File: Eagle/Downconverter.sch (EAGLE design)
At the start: 26 parts, among them J2 3.5HEADPHONEJACK, J5 U.FL_CONN, J6 U.FL_CONN, U1 5V_REG, U2 MIXER, U3 DUAL_OP_AMP_LMV822, U4 DIGITAL_POTDIGITAL_POT

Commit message: update
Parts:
- removed R1: 330, 764Library:R0603
- removed R2: 110, 764Library:R0603
- added C10: 100uF, 764Library:C0603
- added C11: 470pF, 764Library:C0603
- added C9: 10uF, 764Library:C0603
- added R10, R7, R8, R9: 1k, 764Library:R0603
- added U5: TC1185-3.3VCT713, 764Library:TC1185-3.3VCT713
- C3, C4: value 1uF -> 5.6uF
- C8: value 1uF -> 100uF; device 764Library:C0603 -> 764Library:EDK107M6R3A9GAA
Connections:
- removed net N$1: R1.2, R2.1, U1.GND
- removed net N$12: C8.1, U3B.OUT, U4.P0W
- new net AUDIO_OUTPUT: C8.2, J2.RING1, J2.RINGSWITCH, J2.TIP, J2.TIPSWITCH
- new net N$5: C11.1, U5.BYPASS
- net 3.3V: now also C10.1, C6.1, R10.1, R7.1, U3A.VDD, U5.VOUT; no longer J4.2
- net 5V: now also C9.1, U5.!SHDN, U5.VIN; no longer C6.1, R2.2, U3A.VDD
- net 9V: now also J4.2
- net GND: now also C10.2, C11.2, C9.2, R8.2, R9.2, U1.GND, U5.GND; no longer R1.1
- net N$4: now also R7.2, R8.1
- net N$8: now also R10.2, R9.1
- net RDR_OUT: now also C8.1, U3B.OUT, U4.P0W; no longer C8.2, J2.RING1, J2.RINGSWITCH, J2.TIP, J2.TIPSWITCH
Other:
- note added: "TC1185"
- note added: "To Source Module"
- note added: "To the ADC on the DSP Board. Biased on that board."
- note removed: "9V"
- note removed: "From Teensy - Digital Pot 3.3V Power"
- moved on the sheet: J3, J4, J7

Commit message: REV0 and GERBERS FTW
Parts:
- added C12, C13: 0.1uF, 764Library:C0603
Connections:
- net N$2 renamed IF
- net GND: now also C12.2, C13.2
- net N$13: now also R6.1
- net N$4: now also C12.1; no longer R4.1
- net N$8: now also C13.1; no longer R6.1
- net N$9: now also R4.1
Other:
- moved on the sheet: C3, R4, R6, R7, R8, R9

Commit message: Changes
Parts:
- C10, C2: value 100uF -> 1uF
- C3, C4: value 5.6uF -> 2.2uF
- R4, R6: value 1k -> 2.7k
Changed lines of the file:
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@@
 <part name="C1" library="764Library" deviceset="C0603" device="" package3d_urn="urn:adsk.eagle:package:26057/1" value="10uF"/>
 <part name="SUPPLY1" library="SparkFun-PowerSymbols" library_urn="urn:adsk.eagle:library:530" deviceset="5V" device=""/>
-<part name="C2" library="764Library" deviceset="C0603" device="" package3d_urn="urn:adsk.eagle:package:26057/1" value="100uF"/>
+<part name="C2" library="764Library" deviceset="C0603" device="" package3d_urn="urn:adsk.eagle:package:26057/1" value="1uF"/>
 <part name="GND3" library="SparkFun-PowerSymbols" library_urn="urn:adsk.eagle:library:530" deviceset="GND" device=""/>
 <part name="J3" library="SparkFun-Connectors" library_urn="urn:adsk.eagle:library:513" deviceset="CONN_02" device="" package3d_urn="urn:adsk.eagle:package:38039/1"/>
@@
 <part name="R3" library="764Library" deviceset="R0603" device="" package3d_urn="urn:adsk.eagle:package:26057/1" value="50"/>
 <part name="GND8" library="SparkFun-PowerSymbols" library_urn="urn:adsk.eagle:library:530" deviceset="GND" device=""/>
-<part name="C3" library="764Library" deviceset="C0603" device="" package3d_urn="urn:adsk.eagle:package:26057/1" value="5.6uF"/>
-<part name="R4" library="764Library" deviceset="R0603" device="" package3d_urn="urn:adsk.eagle:package:26057/1" value="1k"/>
+<part name="C3" library="764Library" deviceset="C0603" device="" package3d_urn="urn:adsk.eagle:package:26057/1" value="2.2uF"/>
+<part name="R4" library="764Library" deviceset="R0603" device="" package3d_urn="urn:adsk.eagle:package:26057/1" value="2.7k"/>
 <part name="U3" library="764Library" deviceset="DUAL_OP_AMP_LMV822" device=""/>
 <part name="GND9" library="SparkFun-PowerSymbols" library_urn="urn:adsk.eagle:library:530" deviceset="GND" device=""/>
 <part name="R5" library="764Library" deviceset="R0603" device="" package3d_urn="urn:adsk.eagle:package:26057/1" value="100k"/>
-<part name="R6" library="764Library" deviceset="R0603" device="" package3d_urn="urn:adsk.eagle:package:26057/1" value="1k"/>
-<part name="C4" library="764Library" deviceset="C0603" device="" package3d_urn="urn:adsk.eagle:package:26057/1" value="5.6uF"/>
+<part name="R6" library="764Library" deviceset="R0603" device="" package3d_urn="urn:adsk.eagle:package:26057/1" value="2.7k"/>
+<part name="C4" library="764Library" deviceset="C0603" device="" package3d_urn="urn:adsk.eagle:package:26057/1" value="2.2uF"/>
 <part name="C5" library="764Library" deviceset="C0603" device="" package3d_urn="urn:adsk.eagle:package:26057/1" value="330pF"/>
 <part name="U4" library="764Library" deviceset="DIGITAL_POT" device="DIGITAL_POT" package3d_urn="urn:adsk.eagle:package:10501669/1"/>
@@
 <part name="C9" library="764Library" deviceset="C0603" device="" package3d_urn="urn:adsk.eagle:package:26057/1" value="10uF"/>
 <part name="GND18" library="SparkFun-PowerSymbols" library_urn="urn:adsk.eagle:library:530" deviceset="GND" device=""/>
-<part name="C10" library="764Library" deviceset="C0603" device="" package3d_urn="urn:adsk.eagle:package:26057/1" value="100uF"/>
+<part name="C10" library="764Library" deviceset="C0603" device="" package3d_urn="urn:adsk.eagle:package:26057/1" value="1uF"/>
 <part name="GND19" library="SparkFun-PowerSymbols" library_urn="urn:adsk.eagle:library:530" deviceset="GND" device=""/>
 <part name="C11" library="764Library" deviceset="C0603" device="" package3d_urn="urn:adsk.eagle:package:26057/1" value="470pF"/>

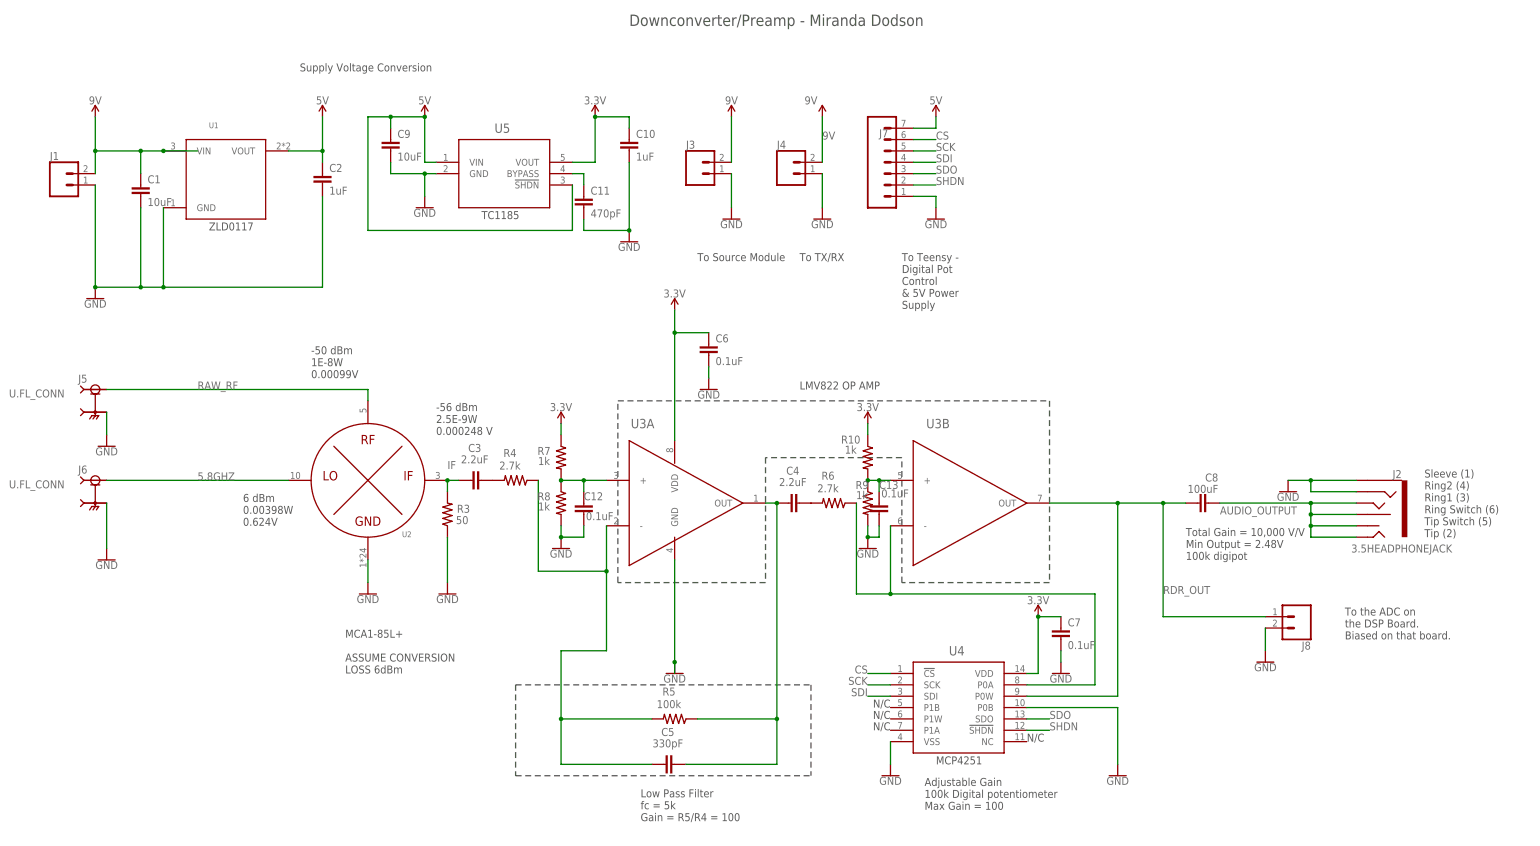
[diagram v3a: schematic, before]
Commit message: Update Schematic to reflect the changes on the radar design
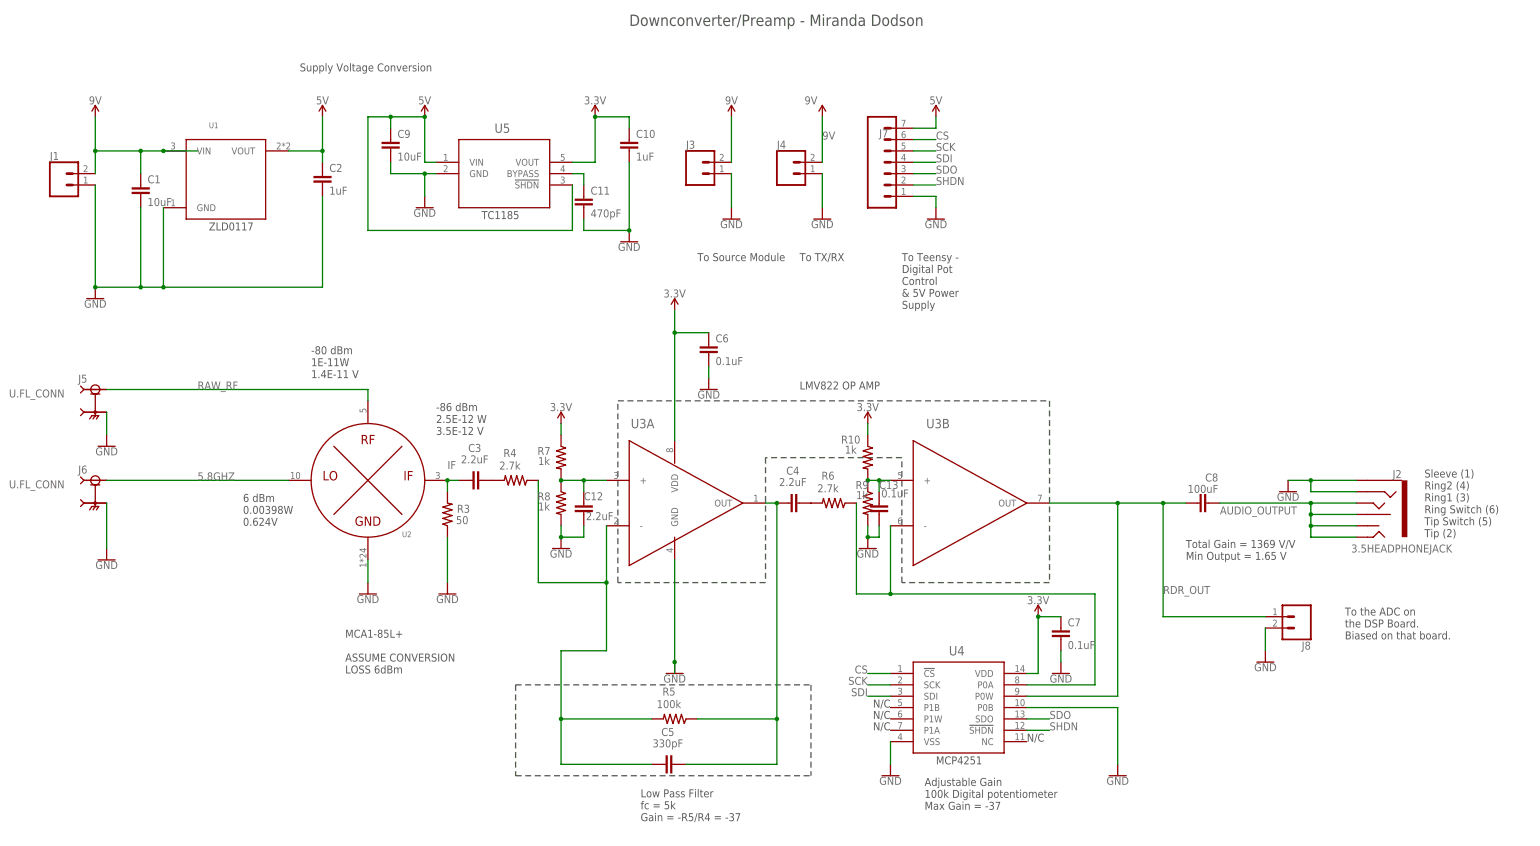
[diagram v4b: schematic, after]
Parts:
- C12: value 0.1uF -> 2.2uF
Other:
- note added: "-80 dBm 1E-11W 1.4E-11 V"
- note added: "-86 dBm 2.5E-12 W 3.5E-12 V"
- note added: "Adjustable Gain 100k Digital potentiometer Max Gain = -37"
- note added: "Low Pass Filter fc = 5k Gain = -R5/R4 = -37"
- note added: "Total Gain = 1369 V/V Min Output = 1.65 V"
- note removed: "-50 dBm 1E-8W 0.00099V"
- note removed: "-56 dBm 2.5E-9W 0.000248 V"
- note removed: "Adjustable Gain 100k Digital potentiometer Max Gain = 100"
- note removed: "Low Pass Filter fc = 5k Gain = R5/R4 = 100"
- note removed: "Total Gain = 10,000 V/V Min Output = 2.48V 100k digipot"
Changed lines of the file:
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@@
 <part name="GND19" library="SparkFun-PowerSymbols" library_urn="urn:adsk.eagle:library:530" deviceset="GND" device=""/>
 <part name="C11" library="764Library" deviceset="C0603" device="" package3d_urn="urn:adsk.eagle:package:26057/1" value="470pF"/>
-<part name="C12" library="764Library" deviceset="C0603" device="" package3d_urn="urn:adsk.eagle:package:26057/1" value="0.1uF"/>
+<part name="C12" library="764Library" deviceset="C0603" device="" package3d_urn="urn:adsk.eagle:package:26057/1" value="2.2uF"/>
 <part name="C13" library="764Library" deviceset="C0603" device="" package3d_urn="urn:adsk.eagle:package:26057/1" value="0.1uF"/>
 </parts>
@@
 <text x="142.24" y="-43.18" size="1.778" layer="97">Low Pass Filter
 fc = 5k
-Gain = R5/R4 = 100</text>
+Gain = -R5/R4 = -37</text>
 <text x="198.12" y="-17.78" size="1.778" layer="97" align="bottom-right">N/C</text>
 <text x="198.12" y="-20.32" size="1.778" layer="97" align="bottom-right">N/C</text>
@@
 <text x="205.74" y="-40.64" size="1.778" layer="97">Adjustable Gain
 100k Digital potentiometer
-Max Gain = 100</text>
-<text x="264.16" y="15.24" size="1.778" layer="97">Total Gain = 10,000 V/V
-Min Output = 2.48V
-100k digipot</text>
+Max Gain = -37</text>
+<text x="264.16" y="15.24" size="1.778" layer="97">Total Gain = 1369 V/V
+Min Output = 1.65 V</text>
 <text x="317.5" y="20.32" size="1.778" layer="97">Sleeve (1)
 Ring2 (4)
@@
 ASSUME CONVERSION
 LOSS 6dBm</text>
-<text x="68.58" y="55.88" size="1.778" layer="97">-50 dBm
-1E-8W
-0.00099V</text>
+<text x="68.58" y="55.88" size="1.778" layer="97">-80 dBm
+1E-11W
+1.4E-11 V</text>
 <text x="53.34" y="22.86" size="1.778" layer="97">6 dBm
 0.00398W
 0.624V</text>
-<text x="96.52" y="43.18" size="1.778" layer="97">-56 dBm
-2.5E-9W
-0.000248 V</text>
+<text x="96.52" y="43.18" size="1.778" layer="97">-86 dBm
+2.5E-12 W
+3.5E-12 V</text>
 <text x="66.04" y="124.46" size="1.778" layer="97">Supply Voltage Conversion</text>
 <wire x1="137.16" y1="50.8" x2="233.68" y2="50.8" width="0.1524" layer="97" style="shortdash"/>
@@
 <junction x="124.46" y="-20.32"/>
 <pinref part="U3" gate="A" pin="-"/>
-<wire x1="134.62" y1="22.86" x2="134.62" y2="12.7" width="0.1524" layer="91"/>
+<wire x1="134.62" y1="22.86" x2="134.62" y2="10.16" width="0.1524" layer="91"/>
 <pinref part="R4" gate="G$1" pin="1"/>
-<wire x1="134.62" y1="12.7" x2="134.62" y2="-5.08" width="0.1524" layer="91"/>
-<wire x1="119.38" y1="33.02" x2="119.38" y2="12.7" width="0.1524" layer="91"/>
-<wire x1="119.38" y1="12.7" x2="134.62" y2="12.7" width="0.1524" layer="91"/>
-<junction x="134.62" y="12.7"/>
-</segment>
-</net>
+<wire x1="134.62" y1="10.16" x2="134.62" y2="-5.08" width="0.1524" layer="91"/>
+<wire x1="119.38" y1="33.02" x2="119.38" y2="10.16" width="0.1524" layer="91"/>
+<wire x1="119.38" y1="10.16" x2="134.62" y2="10.16" width="0.1524" layer="91"/>
+<junction x="134.62" y="10.16"/>
+</segment>
+</net>
